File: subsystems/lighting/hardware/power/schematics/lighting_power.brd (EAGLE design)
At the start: 146.1 x 39.1 mm, 11 parts, among them J1 MOLEX-MICROLOCK-6PIN, J2 MOLEX-MICROLOCK-6PIN, J3 MOLEX-MICROLOCK-6PIN, J4 DCBARRELJACK

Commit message: Lighting V0.3
Fixed daisy-chaining "mirroring" problem
Made DC jack footprint holes smaller (3.3mm->3.1mm dia.)
Made Molex support pads NC
Minor routing updates
Updated silkscreen text
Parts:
- moved J3 0.38 mm to (141.7, 67.6)
- moved J2 0.13 mm to (141.7, 86.9)
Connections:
- net GND: no longer J1.7, J1.8, J2.7, J2.8, J3.7, J3.8
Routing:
- net N$11: track 148.7 -> 126.5 mm
- net GND: track 231.0 -> 209.4 mm, vias 1 -> 3
- net N$14: track 59.8 -> 57.0 mm
- net N$13: track 82.9 -> 80.2 mm, vias 2 -> 0
- net N$15: track 34.8 -> 32.3 mm
- net N$7: track 96.1 -> 95.0 mm
- net N$6: track 119.3 -> 118.6 mm
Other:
- board text added: "PeaPod Lighting Power Board V0.3"
- board text removed: "PeaPod Lighting Power Board V0.2"

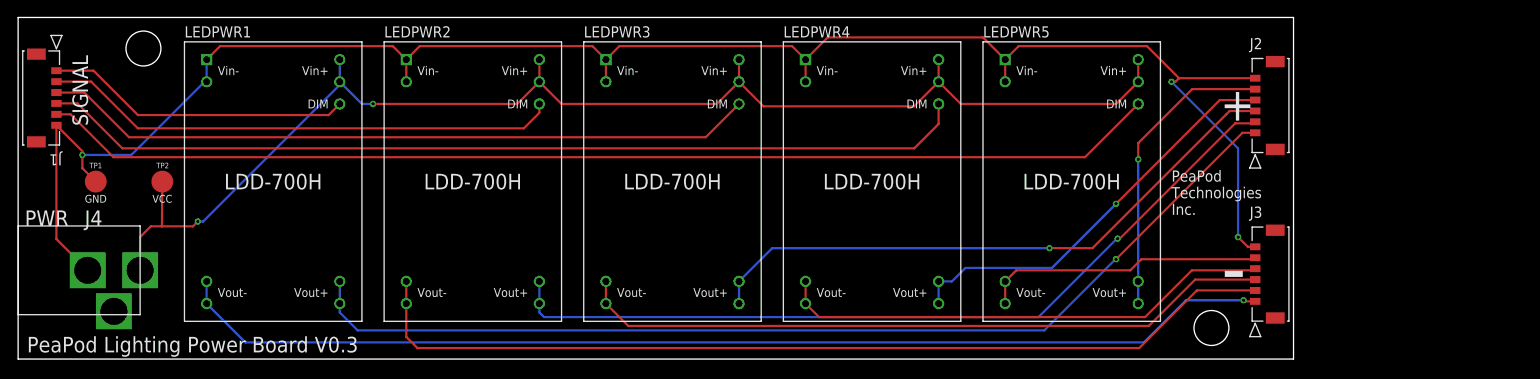
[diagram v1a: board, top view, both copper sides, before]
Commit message: Lighting V0.4
FINALLY fixed the connector flipping error (hint: pin 1 goes to pin 6 EVERY TIME)
Flipped LED series order (blue on bottom)
More "bus"-like routing on power PCB
Updated version number text on PCBs
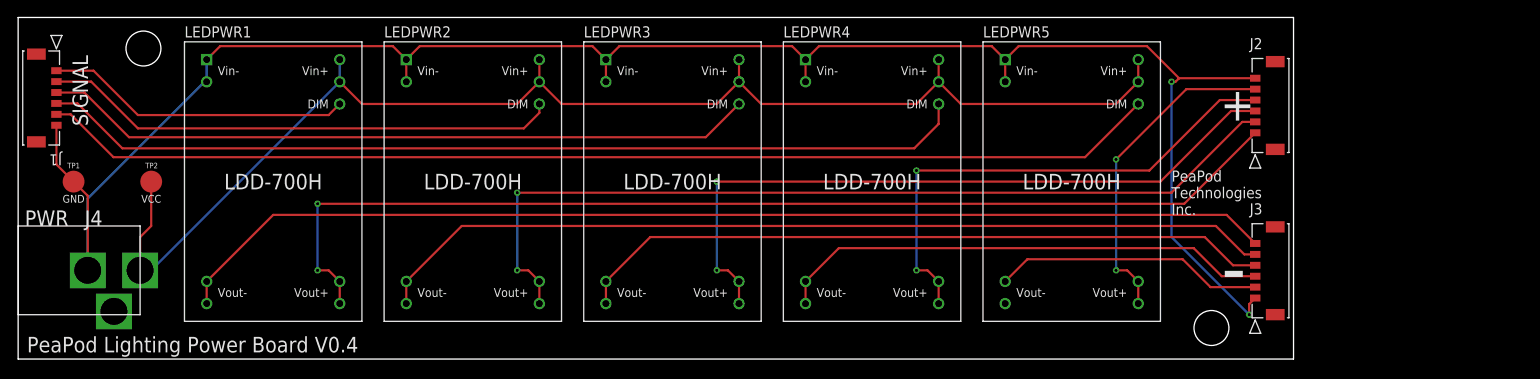
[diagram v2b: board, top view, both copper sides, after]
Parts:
- moved TP1 2.54 mm to (6.35, 81.3)
- moved TP2 1.27 mm to (15.2, 81.3)
- moved J3 0.38 mm to (141.7, 67.9)
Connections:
- net GND: now also J3.1; no longer J3.6
- net N$11: now also J3.6; no longer J3.1
- net N$12: now also J3.5; no longer J3.2
- net N$13: now also J3.4; no longer J3.3
- net N$14: now also J3.3; no longer J3.4
- net N$15: now also J3.2; no longer J3.5
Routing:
- net N$9: track 47.4 -> 59.2 mm, vias 1 -> 2
- net N$8: track 69.7 -> 80.8 mm, vias 1 -> 2
- net GND: track 209.4 -> 219.1 mm, vias 3 -> 2
- net N$7: track 95.0 -> 102.4 mm, vias 1 -> 2
- net N$6: track 118.6 -> 124.0 mm, vias 1 -> 2
- net N$10: track 34.3 -> 37.6 mm, vias 1 -> 2
- net N$12: track 106.8 -> 103.7 mm
- net VCC: track 152.1 -> 155.0 mm, vias 2 -> 0
- net N$15: track 32.3 -> 31.0 mm
- net N$11: track 126.5 -> 127.1 mm, vias 1 -> 0
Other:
- board text added: "PeaPod Lighting Power Board V0.4"
- board text removed: "PeaPod Lighting Power Board V0.3"

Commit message: Power V0.5 - Module Update
Replaced discontinued module (LDD-H) with SMD package variant (LDD-HS; same functionality)
Board and mount resized, components repositioned
Added PWM pull-down resistors
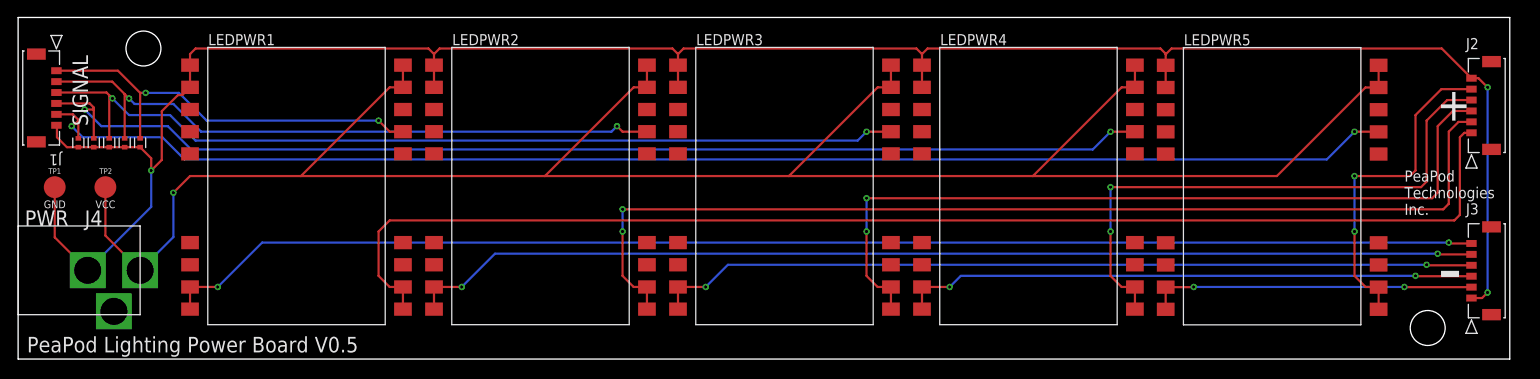
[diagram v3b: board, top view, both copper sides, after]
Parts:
- added R1, R2, R3, R4, R5: 10k, Resistor:RESC1005X40
- LEDPWR1, LEDPWR2, LEDPWR3, LEDPWR4, LEDPWR5: value LDD-700H -> LDD-500HS; device MeanWell NLDD-H Series:NLDD-300~1000H -> MeanWell NLDD-H Series:LDD-300~1000HS
- moved J2 24.8 mm to (166.4, 86.9)
- moved J3 24.8 mm to (166.4, 67.9)
- moved LEDPWR5 17.1 mm to (131.4, 94.6), turned to 270 degrees
- moved LEDPWR1 16.4 mm to (19.7, 94.6), turned to 270 degrees
- moved LEDPWR4 14.5 mm to (103.5, 94.6), turned to 270 degrees
- moved LEDPWR2 14.1 mm to (47.6, 94.6), turned to 270 degrees
- moved LEDPWR3 13.4 mm to (75.6, 94.6), turned to 270 degrees
- moved TP2 5.29 mm to (9.99, 80.6)
- moved TP1 2.25 mm to (4.19, 80.6)
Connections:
- removed net N$10: J2.5, LEDPWR5.VO+1, LEDPWR5.VO+2
- removed net N$11: J3.6, LEDPWR1.VO-1, LEDPWR1.VO-2
- removed net N$12: J3.5, LEDPWR2.VO-1, LEDPWR2.VO-2
- removed net N$13: J3.4, LEDPWR3.VO-1, LEDPWR3.VO-2
- removed net N$14: J3.3, LEDPWR4.VO-1, LEDPWR4.VO-2
- removed net N$15: J3.2, LEDPWR5.VO-1, LEDPWR5.VO-2
- removed net N$6: J2.1, LEDPWR1.VO+1, LEDPWR1.VO+2
- removed net N$7: J2.2, LEDPWR2.VO+1, LEDPWR2.VO+2
- removed net N$8: J2.3, LEDPWR3.VO+1, LEDPWR3.VO+2
- removed net N$9: J2.4, LEDPWR4.VO+1, LEDPWR4.VO+2
- new net BLUE+: J2.1, LEDPWR1.P$13, LEDPWR1.P$14
- new net BLUE-: J3.6, LEDPWR1.P$11, LEDPWR1.P$12
- new net COOL+: J2.2, LEDPWR2.P$13, LEDPWR2.P$14
- new net COOL-: J3.5, LEDPWR2.P$11, LEDPWR2.P$12
- new net FAR+: J2.5, LEDPWR5.P$13, LEDPWR5.P$14
- new net FAR-: J3.2, LEDPWR5.P$11, LEDPWR5.P$12
- new net RED+: J2.4, LEDPWR4.P$13, LEDPWR4.P$14
- new net RED-: J3.3, LEDPWR4.P$11, LEDPWR4.P$12
- new net WARM+: J2.3, LEDPWR3.P$13, LEDPWR3.P$14
- new net WARM-: J3.4, LEDPWR3.P$11, LEDPWR3.P$12
- net GND: now also LEDPWR1.P$1, LEDPWR1.P$2, LEDPWR2.P$1, LEDPWR2.P$2, LEDPWR3.P$1, LEDPWR3.P$2, LEDPWR4.P$1, LEDPWR4.P$2, LEDPWR5.P$1, LEDPWR5.P$2, R1.2, R2.2, R3.2, R4.1, R5.1; no longer LEDPWR1.VIN-1, LEDPWR1.VIN-2, LEDPWR2.VIN-1, LEDPWR2.VIN-2, LEDPWR3.VIN-1, LEDPWR3.VIN-2, LEDPWR4.VIN-1, LEDPWR4.VIN-2, LEDPWR5.VIN-1, LEDPWR5.VIN-2
- net N$1: now also LEDPWR1.P$21, R1.1; no longer LEDPWR1.DIM
- net N$2: now also LEDPWR2.P$21, R2.1; no longer LEDPWR2.DIM
- net N$3: now also LEDPWR3.P$21, R3.1; no longer LEDPWR3.DIM
- net N$4: now also LEDPWR4.P$21, R4.2; no longer LEDPWR4.DIM
- net N$5: now also LEDPWR5.P$21, R5.2; no longer LEDPWR5.DIM
- net VCC: now also LEDPWR1.P$23, LEDPWR1.P$24, LEDPWR2.P$23, LEDPWR2.P$24, LEDPWR3.P$23, LEDPWR3.P$24, LEDPWR4.P$23, LEDPWR4.P$24, LEDPWR5.P$23, LEDPWR5.P$24; no longer LEDPWR1.VIN+1, LEDPWR1.VIN+2, LEDPWR2.VIN+1, LEDPWR2.VIN+2, LEDPWR3.VIN+1, LEDPWR3.VIN+2, LEDPWR4.VIN+1, LEDPWR4.VIN+2, LEDPWR5.VIN+1, LEDPWR5.VIN+2
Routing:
- net BLUE-: track 0.00 -> 151.4 mm, vias 0 -> 2
- net BLUE+: track 0.00 -> 146.0 mm
- net N$11: track 127.1 -> 0.00 mm
- net N$6: track 124.0 -> 0.00 mm, vias 2 -> 0
- net COOL-: track 0.00 -> 123.0 mm, vias 0 -> 2
- net COOL+: track 0.00 -> 119.7 mm, vias 0 -> 2
- net N$12: track 103.7 -> 0.00 mm
- net N$7: track 102.4 -> 0.00 mm, vias 2 -> 0
- net WARM-: track 0.00 -> 94.5 mm, vias 0 -> 2
- net WARM+: track 0.00 -> 92.6 mm, vias 0 -> 2
- net VCC: track 155.0 -> 240.9 mm, vias 0 -> 1
- net N$8: track 80.8 -> 0.00 mm, vias 2 -> 0
- net N$13: track 80.3 -> 0.00 mm
- net RED-: track 0.00 -> 66.0 mm, vias 0 -> 2
- net RED+: track 0.00 -> 65.6 mm, vias 0 -> 2
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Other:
- board size 146.1 x 39.1 mm -> 170.8 x 39.1 mm
- board text added: "PeaPod Lighting Power Board V0.5"
- board text removed: "PeaPod Lighting Power Board V0.4"
